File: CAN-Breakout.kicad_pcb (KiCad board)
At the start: 2 copper layers, 58.1 x 33.5 mm, 37 parts, among them J1 USB_C_Receptacle_USB2.0_16P, J2 DE9_Pins, U1 ESP32-C6-MINI-1/U, U3 TLV70033_SOT23-5, U4 CDSOT23-T24CAN, U5 TCAN337, U6 USBLC6-2SC6

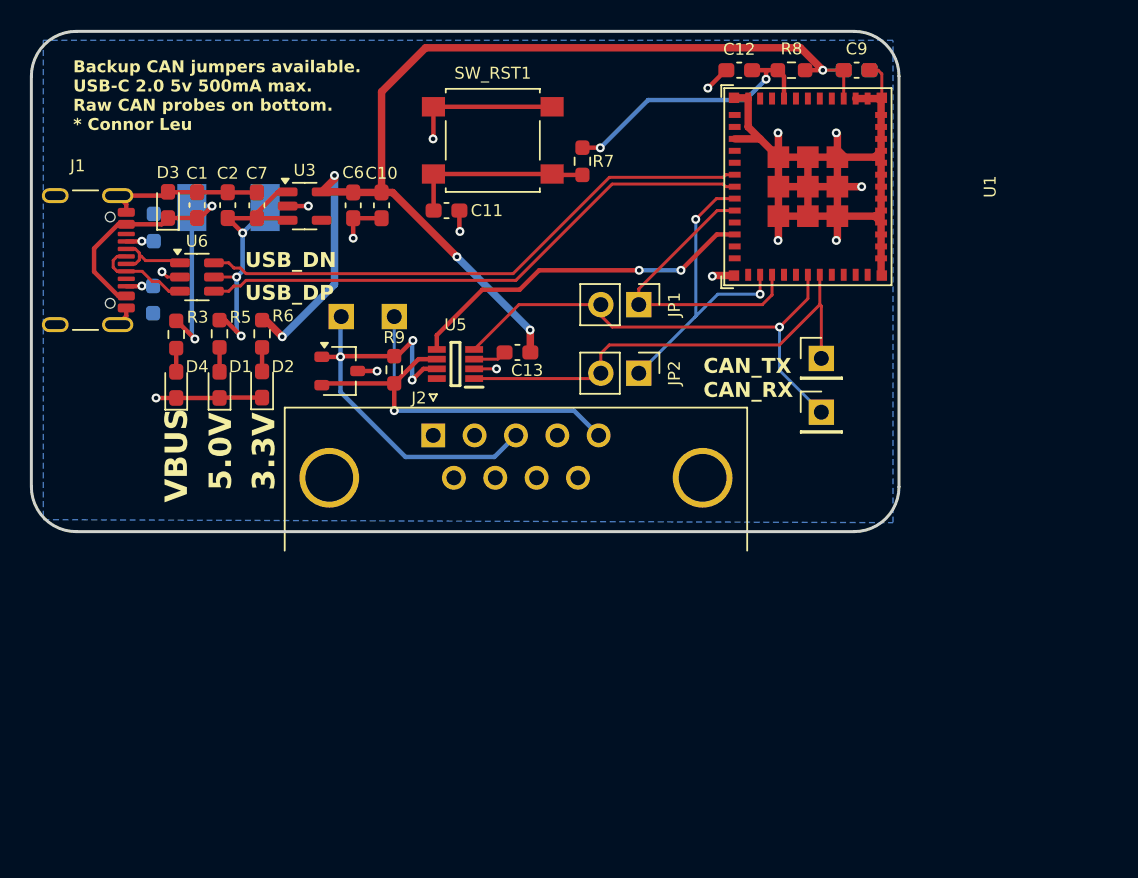
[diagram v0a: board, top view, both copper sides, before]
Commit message: redo layout its smaller
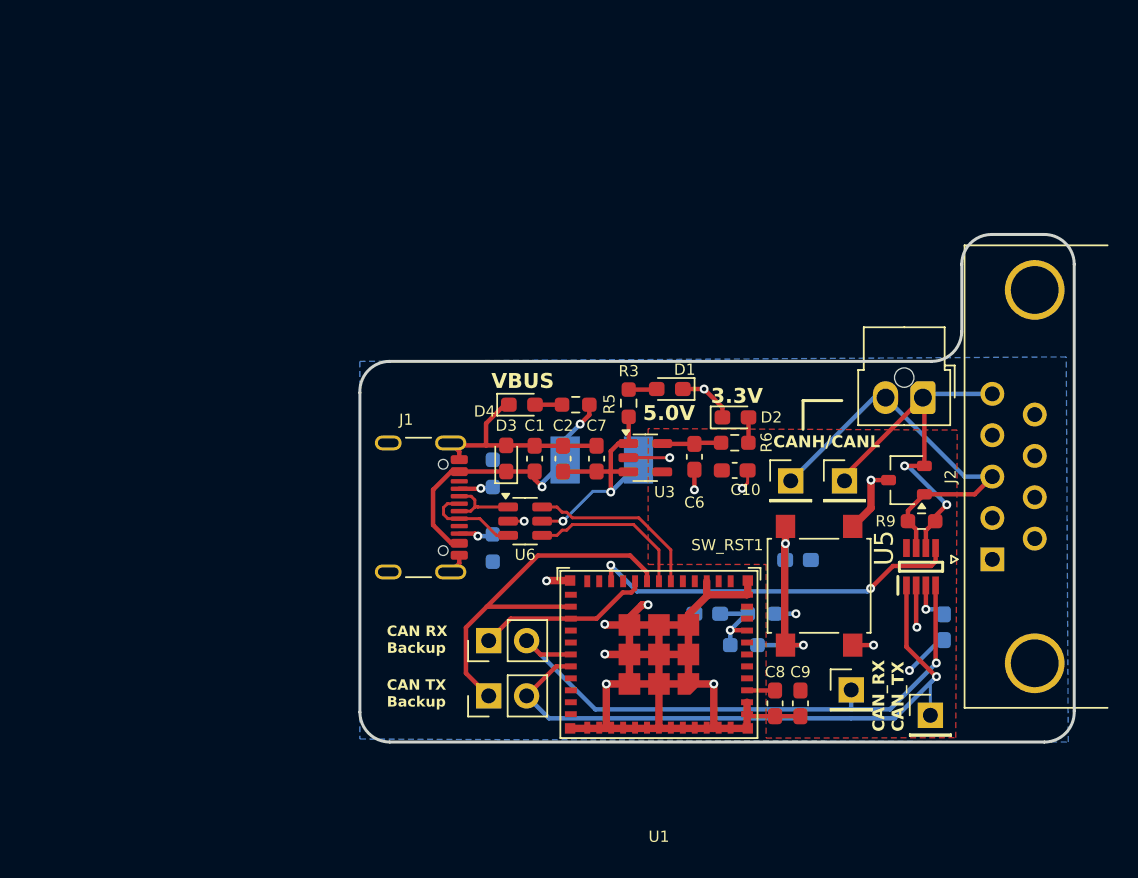
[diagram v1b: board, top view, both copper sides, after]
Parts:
- added J3: Conn_01x02_Pin, Connector_Molex:Molex_Nano-Fit_105309-xx02_1x02_P2.50mm_Vertical, F.Cu at (135.6, 115.5)
- C11, C12, C13, R7, R8: moved to B.Cu
- C8, TP3, TP4: moved to F.Cu
- moved C8 42.8 mm to (125.7, 136.0), turned to -90 degrees
- moved C9 42.6 mm to (127.4, 136.0), turned to -90 degrees
- moved U4 38.6 mm to (134.5, 121.0), turned to 180 degrees
- moved J2 38.3 mm to (140.2, 126.4), turned to 90 degrees
- moved SW_RST1 37.0 mm to (128.7, 128.1), turned to -90 degrees
- moved R9 36.7 mm to (135.5, 123.8), turned to 0 degrees
- moved C12 36.5 mm to (121.2, 130.0)
- moved R8 36.5 mm to (124.8, 130.0)
- moved U1 36.3 mm to (117.9, 135.4), turned to 180 degrees
- moved R7 34.2 mm to (123.6, 132.1), turned to 180 degrees
- moved U5 34.0 mm to (135.5, 126.8), turned to 90 degrees
- moved C13 34.0 mm to (137.0, 130.9), turned to -90 degrees
- moved C11 33.2 mm to (127.2, 126.4)
- moved R6 32.5 mm to (123.0, 118.5), turned to 180 degrees
- moved TP3 32.1 mm to (130.3, 121.1), turned to 0 degrees
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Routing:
- net +3V3: track 78.8 -> 10.4 mm, vias 5 -> 2
- net USB_DP: track 37.9 -> 10.9 mm
- net USB_DN: track 37.9 -> 11.9 mm
- net Net-(U1-EN/CHIP_PU): track 18.6 -> 5.62 mm, vias 2 -> 1
- net CAN_TXD: track 31.6 -> 42.7 mm, vias 0 -> 1
- net CAN_RXD_BKP1: track 20.2 -> 11.7 mm
- net CAN_RXD: track 33.9 -> 40.5 mm
- net VBUS: track 25.5 -> 20.0 mm
- net CANL: track 30.9 -> 25.8 mm, vias 1 -> 2
- net CAN_TXD_BKP1: track 21.4 -> 26.0 mm, vias 2 -> 0
- net CANH: track 30.4 -> 27.3 mm, vias 3 -> 0
- net +5V: track 21.4 -> 18.7 mm, vias 3 -> 2
- net GND: track 104.5 -> 102.7 mm, vias 15 -> 14
- net CAN_FAULT: track 23.7 -> 25.3 mm
- net Net-(SW_RST1-B): track 12.5 -> 13.4 mm, vias 0 -> 2
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- added copper zone on F.Cu, net +3V3
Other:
- board size 58.1 x 33.5 mm -> 47.8 x 34 mm
- board text added: "CAN RX Backup"
- board text added: "CAN TX Backup"
- board text added: "CANH/CANL"
- board text added: "CAN_RX CAN_TX"
- board text removed: "Backup CAN jumpers available. USB-C 2.0 5v 500mA max. Raw CAN probes on bottom. * Connor Leu"
- board text removed: "CANH CANL"
- board text removed: "CAN_TX CAN_RX"
- board text removed: "USB_DN"
- board text removed: "USB_DP"
